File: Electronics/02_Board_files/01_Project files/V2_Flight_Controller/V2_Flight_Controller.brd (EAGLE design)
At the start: 40 x 40 mm, 75 parts

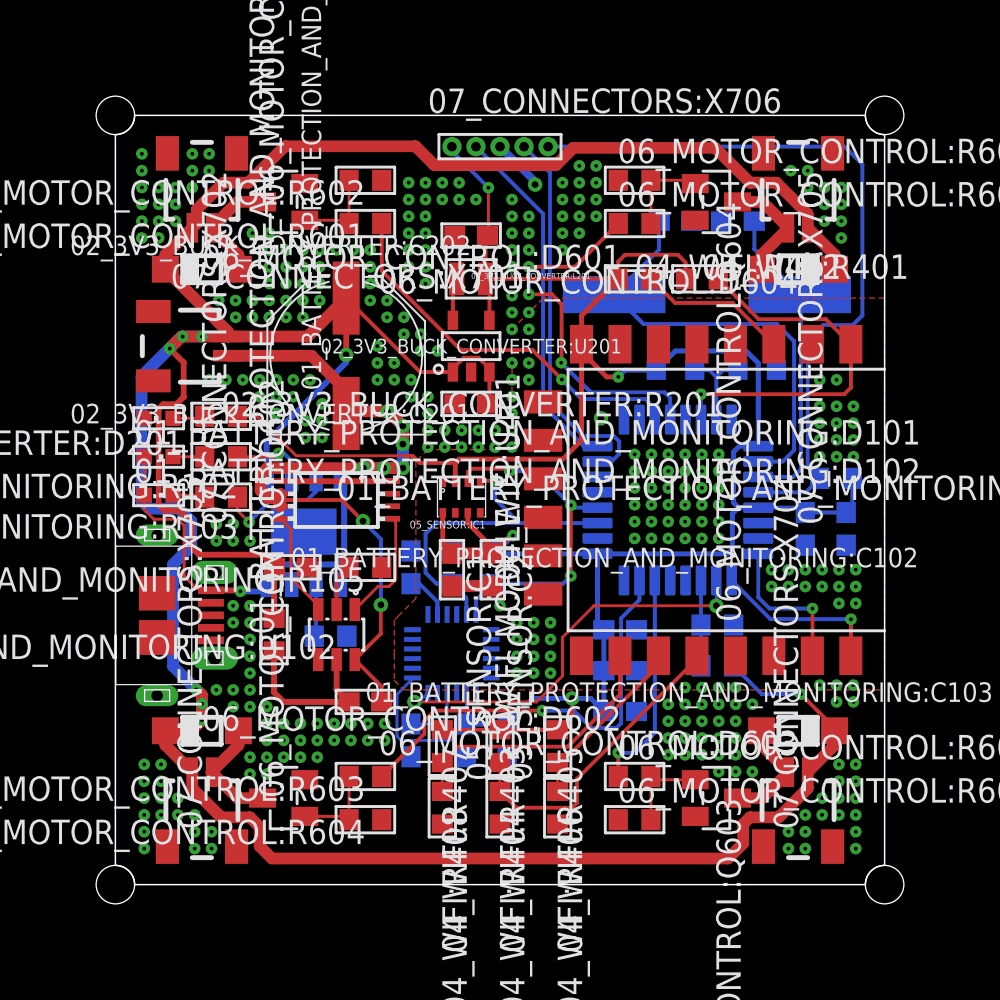
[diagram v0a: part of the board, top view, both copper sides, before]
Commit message: 1. Added libraries 2. Renamed GND vias 3. Created GND polygons
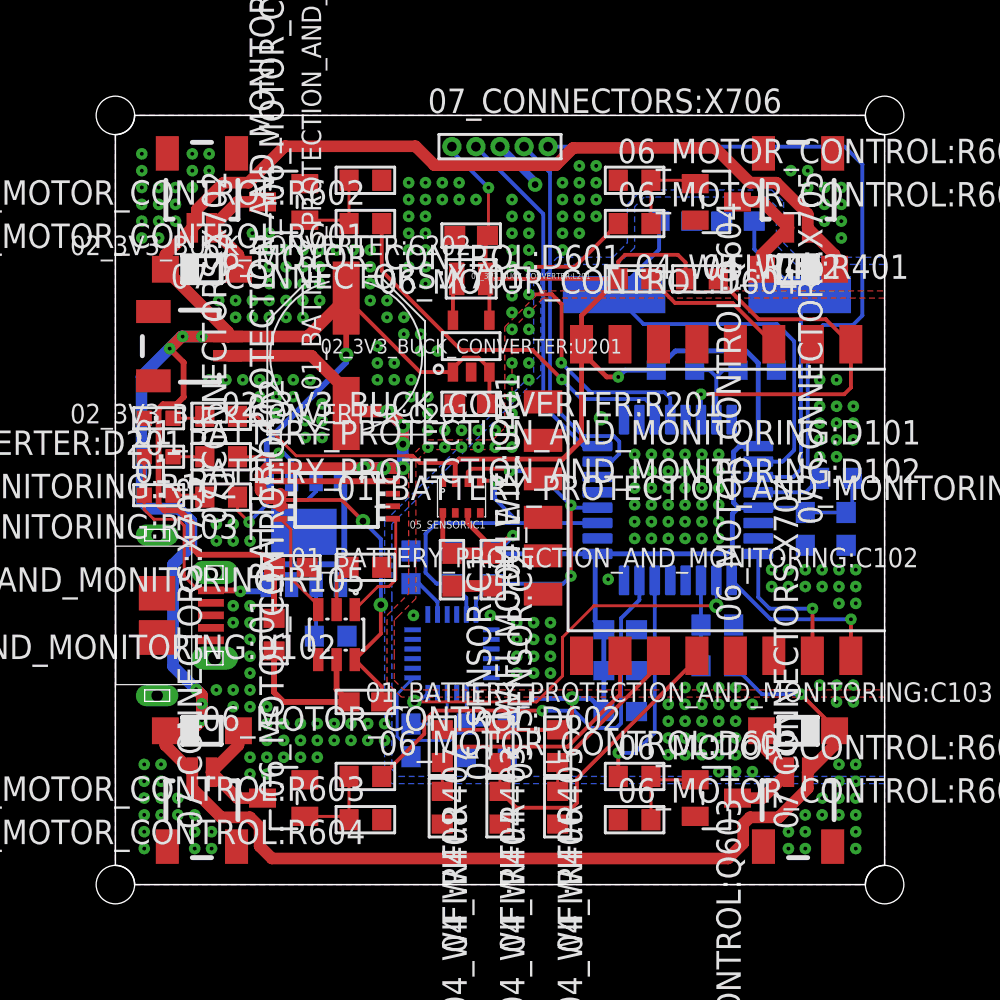
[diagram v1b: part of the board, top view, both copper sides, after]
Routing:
- net GND: vias 26 -> 343
- added copper zone on layer 16, net GND

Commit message: 1. Removed all DRC errors
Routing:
- net GND: vias 343 -> 350
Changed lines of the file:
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@@
 <wire x1="19.625" y1="15.65" x2="18.75" y2="14.775" width="0.2" layer="16"/>
 <wire x1="18.75" y1="14.775" x2="18.75" y2="14.0462" width="0.2" layer="16"/>
-<wire x1="19.625" y1="15.65" x2="23.2844" y2="15.65" width="0.2" layer="16"/>
-<wire x1="23.2844" y1="15.65" x2="23.6844" y2="16.05" width="0.2" layer="16"/>
-<via x="23.6844" y="16.05" extent="1-16" drill="0.2" diameter="0.45"/>
-<wire x1="23.6844" y1="16.05" x2="23.6844" y2="19.725" width="0.2" layer="1"/>
-<via x="23.6844" y="19.725" extent="1-16" drill="0.2" diameter="0.45"/>
-<wire x1="23.6844" y1="19.725" x2="23.8094" y2="19.6" width="0.2" layer="16"/>
-<wire x1="23.8094" y1="19.6" x2="25.07" y2="19.6" width="0.2" layer="16"/>
+<via x="23.75" y="16.05" extent="1-16" drill="0.2" diameter="0.45"/>
 <contactref element="05_SENSOR:IC1" pad="3"/>
 <via x="20.5" y="21.5" extent="1-16" drill="0.2" diameter="0.45"/>
-<wire x1="20.5" y1="21.5" x2="21.9094" y2="21.5" width="0.2" layer="16"/>
-<wire x1="21.9094" y1="21.5" x2="23.6844" y2="19.725" width="0.2" layer="16"/>
 <wire x1="20.5" y1="21.5" x2="20.375" y2="21.625" width="0.2" layer="1"/>
 <wire x1="18.325" y1="21.45" x2="18.325" y2="20.925" width="0.2" layer="1"/>
 <wire x1="20.375" y1="21.625" x2="18.5" y2="21.625" width="0.2" layer="1"/>
 <wire x1="18.5" y1="21.625" x2="18.325" y2="21.45" width="0.2" layer="1"/>
+<via x="23.75" y="19.75" extent="1-16" drill="0.2" diameter="0.45"/>
+<wire x1="23.75" y1="19.75" x2="23.9" y2="19.6" width="0.2" layer="16"/>
+<wire x1="23.9" y1="19.6" x2="25.07" y2="19.6" width="0.2" layer="16"/>
+<wire x1="23.75" y1="19.75" x2="22.25" y2="19.75" width="0.2" layer="16"/>
+<wire x1="22.25" y1="19.75" x2="20.5" y2="21.5" width="0.2" layer="16"/>
+<wire x1="23.75" y1="19.75" x2="23.75" y2="16.05" width="0.2" layer="1"/>
+<wire x1="23.35" y1="15.65" x2="23.75" y2="16.05" width="0.2" layer="16"/>
+<wire x1="19.625" y1="15.65" x2="23.35" y2="15.65" width="0.2" layer="16"/>
 </signal>
 <signal name="BATTERY_+VE">
@@
 </polygon>
 <via x="25.625" y="15.875" extent="1-16" drill="0.2" diameter="0.45"/>
-<wire x1="29.975" y1="34.5" x2="30.15" y2="34.55" width="0" layer="19" extent="1-16"/>
-<wire x1="9.975" y1="16.5" x2="9.165" y2="15.6" width="0" layer="19" extent="1-16"/>
+<via x="30.375" y="33.125" extent="1-16" drill="0.2" diameter="0.45"/>
+<via x="31.25" y="33.125" extent="1-16" drill="0.2" diameter="0.45"/>
+<via x="32.125" y="33.125" extent="1-16" drill="0.2" diameter="0.45"/>
+<via x="12.875" y="17.75" extent="1-16" drill="0.2" diameter="0.45"/>
+<via x="15.5" y="20.75" extent="1-16" drill="0.2" diameter="0.45"/>
+<via x="15.5" y="19.875" extent="1-16" drill="0.2" diameter="0.45"/>
+<via x="15.5" y="19" extent="1-16" drill="0.2" diameter="0.45"/>
 </signal>
 <signal name="M2_PWM">
